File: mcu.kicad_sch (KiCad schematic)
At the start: 29 parts, among them J7 CONN_MCU_SERIAL, SW1 SW_RST, SW2 SW_BOOT0, U2 STM32F765IITx, Y2 25MHz

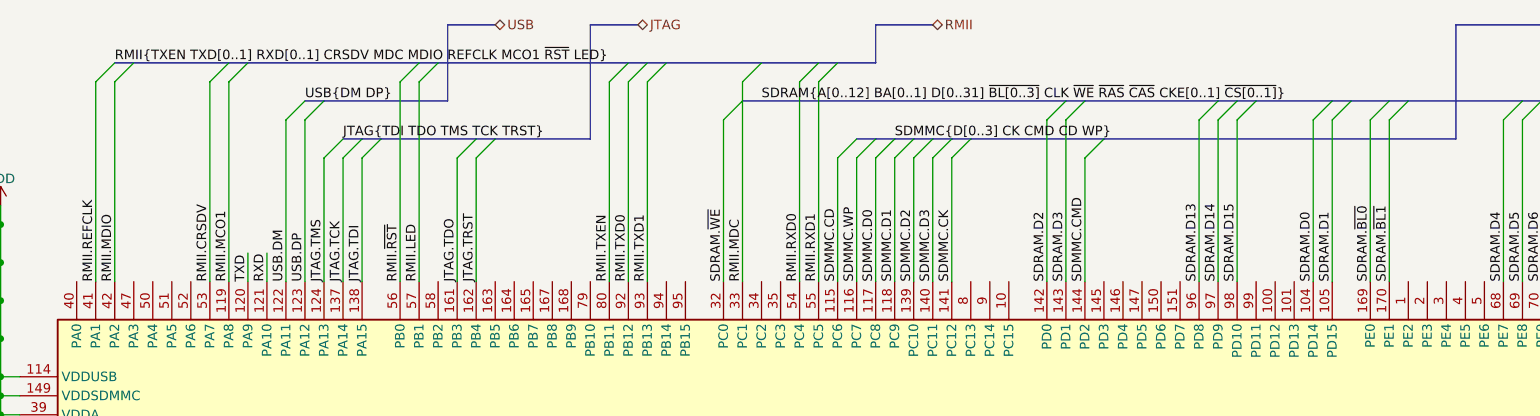
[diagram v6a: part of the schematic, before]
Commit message: Add display connector
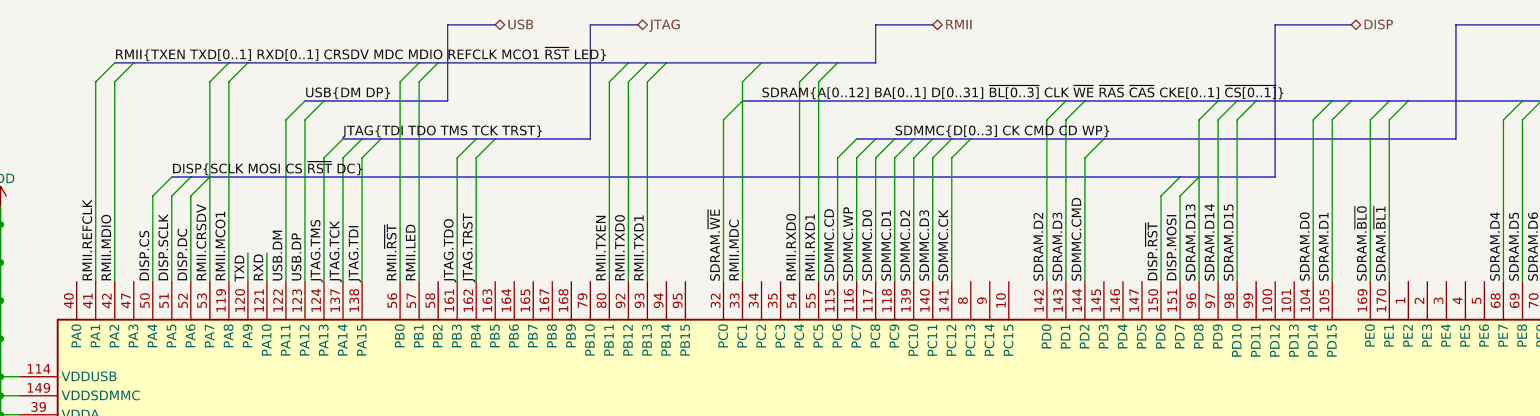
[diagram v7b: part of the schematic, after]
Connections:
- net DISP.~{RST}: now reaches U2.150 (PD6)
- net DISP.MOSI: now reaches U2.151 (PD7)
- net DISP.CS: now reaches U2.50 (PA4)
- net DISP.SCLK: now reaches U2.51 (PA5)
- net DISP.DC: now reaches U2.52 (PA6)
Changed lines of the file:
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@@
+    (stroke (width 0) (type default) (color 0 0 0 0))
+  )
+  (bus_entry (at 201.93 36.83) (size -2.54 2.54)
+    (stroke (width 0) (type default) (color 0 0 0 0))
+  )
+  (bus_entry (at 199.39 36.83) (size -2.54 2.54)
     (stroke (width 0) (type default) (color 0 0 0 0))
   )
@@
     (stroke (width 0) (type default) (color 0 0 0 0))
   )
+  (bus_entry (at 69.85 36.83) (size -2.54 2.54)
+    (stroke (width 0) (type default) (color 0 0 0 0))
+  )
   (bus_entry (at 189.23 31.75) (size -2.54 2.54)
     (stroke (width 0) (type default) (color 0 0 0 0))
@@
     (stroke (width 0) (type default) (color 0 0 0 0))
   )
+  (bus_entry (at 64.77 36.83) (size -2.54 2.54)
+    (stroke (width 0) (type default) (color 0 0 0 0))
+  )
   (bus_entry (at 153.67 144.78) (size 2.54 2.54)
     (stroke (width 0) (type default) (color 0 0 0 0))
@@
     (stroke (width 0) (type default) (color 0 0 0 0))
   )
+  (bus_entry (at 67.31 36.83) (size -2.54 2.54)
+    (stroke (width 0) (type default) (color 0 0 0 0))
+  )
   (bus_entry (at 158.75 31.75) (size -2.54 2.54)
     (stroke (width 0) (type default) (color 0 0 0 0))
@@
     (stroke (width 0) (type default) (color 0 0 0 0))
   )
-  (wire (pts (xy 69.85 24.13) (xy 69.85 50.8))
+  (wire (pts (xy 69.85 24.13) (xy 69.85 36.83))
     (stroke (width 0) (type default) (color 0 0 0 0))
   )
@@
     (stroke (width 0) (type default) (color 0 0 0 0))
   )
+  (wire (pts (xy 62.23 39.37) (xy 62.23 50.8))
+    (stroke (width 0) (type default) (color 0 0 0 0))
+  )
   (wire (pts (xy 22.86 78.74) (xy 25.4 78.74))
     (stroke (width 0) (type default) (color 0 0 0 0))
@@
     (stroke (width 0) (type default) (color 0 0 0 0))
   )
+  (bus (pts (xy 201.93 36.83) (xy 212.09 36.83))
+    (stroke (width 0) (type default) (color 0 0 0 0))
+  )
   (wire (pts (xy 191.77 124.46) (xy 191.77 144.78))
     (stroke (width 0) (type default) (color 0 0 0 0))
@@
     (stroke (width 0) (type default) (color 0 0 0 0))
   )
+  (wire (pts (xy 199.39 39.37) (xy 199.39 50.8))
+    (stroke (width 0) (type default) (color 0 0 0 0))
+  )
   (wire (pts (xy 22.86 104.14) (xy 30.48 104.14))
     (stroke (width 0) (type default) (color 0 0 0 0))
   )
+  (bus (pts (xy 67.31 36.83) (xy 69.85 36.83))
+    (stroke (width 0) (type default) (color 0 0 0 0))
+  )
   (wire (pts (xy 38.1 63.5) (xy 41.91 63.5))
     (stroke (width 0) (type default) (color 0 0 0 0))
@@
     (stroke (width 0) (type default) (color 0 0 0 0))
   )
+  (wire (pts (xy 64.77 39.37) (xy 64.77 50.8))
+    (stroke (width 0) (type default) (color 0 0 0 0))
+  )
   (wire (pts (xy 57.15 24.13) (xy 57.15 50.8))
     (stroke (width 0) (type default) (color 0 0 0 0))
@@
     (stroke (width 0) (type default) (color 0 0 0 0))
   )
-  (wire (pts (xy 201.93 29.21) (xy 201.93 50.8))
+  (wire (pts (xy 201.93 29.21) (xy 201.93 36.83))
     (stroke (width 0) (type default) (color 0 0 0 0))
   )
@@
     (stroke (width 0) (type default) (color 0 0 0 0))
   )
+  (bus (pts (xy 69.85 36.83) (xy 199.39 36.83))
+    (stroke (width 0) (type default) (color 0 0 0 0))
+  )
   (wire (pts (xy 166.37 124.46) (xy 166.37 144.78))
     (stroke (width 0) (type default) (color 0 0 0 0))
@@
     (stroke (width 0) (type default) (color 0 0 0 0))
   )
+  (bus (pts (xy 212.09 36.83) (xy 212.09 16.51))
+    (stroke (width 0) (type default) (color 0 0 0 0))
+  )
   (wire (pts (xy 252.73 124.46) (xy 252.73 144.78))
     (stroke (width 0) (type default) (color 0 0 0 0))
@@
     (stroke (width 0) (type default) (color 0 0 0 0))
   )
+  (wire (pts (xy 201.93 36.83) (xy 201.93 50.8))
+    (stroke (width 0) (type default) (color 0 0 0 0))
+  )
   (wire (pts (xy 82.55 29.21) (xy 82.55 50.8))
     (stroke (width 0) (type default) (color 0 0 0 0))
@@
     (stroke (width 0) (type default) (color 0 0 0 0))
   )
+  (bus (pts (xy 212.09 16.51) (xy 222.25 16.51))
+    (stroke (width 0) (type default) (color 0 0 0 0))
+  )
   (wire (pts (xy 234.95 124.46) (xy 234.95 144.78))
     (stroke (width 0) (type default) (color 0 0 0 0))
@@
     (stroke (width 0) (type default) (color 0 0 0 0))
   )
+  (bus (pts (xy 199.39 36.83) (xy 201.93 36.83))
+    (stroke (width 0) (type default) (color 0 0 0 0))
+  )
   (wire (pts (xy 27.94 151.13) (xy 27.94 171.45))
     (stroke (width 0) (type default) (color 0 0 0 0))
@@
     (stroke (width 0) (type default) (color 0 0 0 0))
   )
+  (wire (pts (xy 196.85 39.37) (xy 196.85 50.8))
+    (stroke (width 0) (type default) (color 0 0 0 0))
+  )
   (bus (pts (xy 229.87 26.67) (xy 245.11 26.67))
     (stroke (width 0) (type default) (color 0 0 0 0))
@@
     (stroke (width 0) (type default) (color 0 0 0 0))
   )
+  (wire (pts (xy 67.31 39.37) (xy 67.31 50.8))
+    (stroke (width 0) (type default) (color 0 0 0 0))
+  )
   (wire (pts (xy 41.91 66.04) (xy 41.91 68.58))
     (stroke (width 0) (type default) (color 0 0 0 0))
@@
     (stroke (width 0) (type default) (color 0 0 0 0))
   )
+  (bus (pts (xy 64.77 36.83) (xy 67.31 36.83))
+    (stroke (width 0) (type default) (color 0 0 0 0))
+  )
   (bus (pts (xy 158.75 147.32) (xy 161.29 147.32))
     (stroke (width 0) (type default) (color 0 0 0 0))
@@
     (stroke (width 0) (type default) (color 0 0 0 0))
   )
+  (wire (pts (xy 69.85 36.83) (xy 69.85 50.8))
+    (stroke (width 0) (type default) (color 0 0 0 0))
+  )
   (wire (pts (xy 270.51 78.74) (xy 274.32 78.74))
     (stroke (width 0) (type default) (color 0 0 0 0))
@@
     (effects (font (size 1.27 1.27)) (justify left bottom))
   )
+  (label "DISP{SCLK MOSI CS ~{RST} DC}" (at 64.77 36.83 0)
+    (effects (font (size 1.27 1.27)) (justify left bottom))
+  )
   (label "RMII.RXD0" (at 148.59 50.8 90)
     (effects (font (size 1.27 1.27)) (justify left bottom))
@@
   )
   (label "SDRAM.D7" (at 250.19 50.8 90)
+    (effects (font (size 1.27 1.27)) (justify left bottom))
+  )
+  (label "DISP.~{RST}" (at 196.85 50.8 90)
+    (effects (font (size 1.27 1.27)) (justify left bottom))
+  )
+  (label "DISP.MOSI" (at 199.39 50.8 90)
     (effects (font (size 1.27 1.27)) (justify left bottom))
   )
@@
     (effects (font (size 1.27 1.27)) (justify right bottom))
   )
+  (label "DISP.SCLK" (at 64.77 50.8 90)
+    (effects (font (size 1.27 1.27)) (justify left bottom))
+  )
   (label "SDRAM.D5" (at 245.11 50.8 90)
     (effects (font (size 1.27 1.27)) (justify left bottom))
@@
     (effects (font (size 1.27 1.27)) (justify right bottom))
   )
+  (label "DISP.DC" (at 67.31 50.8 90)
+    (effects (font (size 1.27 1.27)) (justify left bottom))
+  )
   (label "SDRAM.D22" (at 173.99 124.46 270)
     (effects (font (size 1.27 1.27)) (justify right bottom))
@@
   )
   (label "SDRAM.D10" (at 257.81 50.8 90)
+    (effects (font (size 1.27 1.27)) (justify left bottom))
+  )
+  (label "DISP.CS" (at 62.23 50.8 90)
     (effects (font (size 1.27 1.27)) (justify left bottom))
   )
@@
     (effects (font (size 1.27 1.27)) (justify left))
   )
+  (hierarchical_label "DISP" (shape bidirectional) (at 222.25 16.51 0)
+    (effects (font (size 1.27 1.27)) (justify left))
+  )

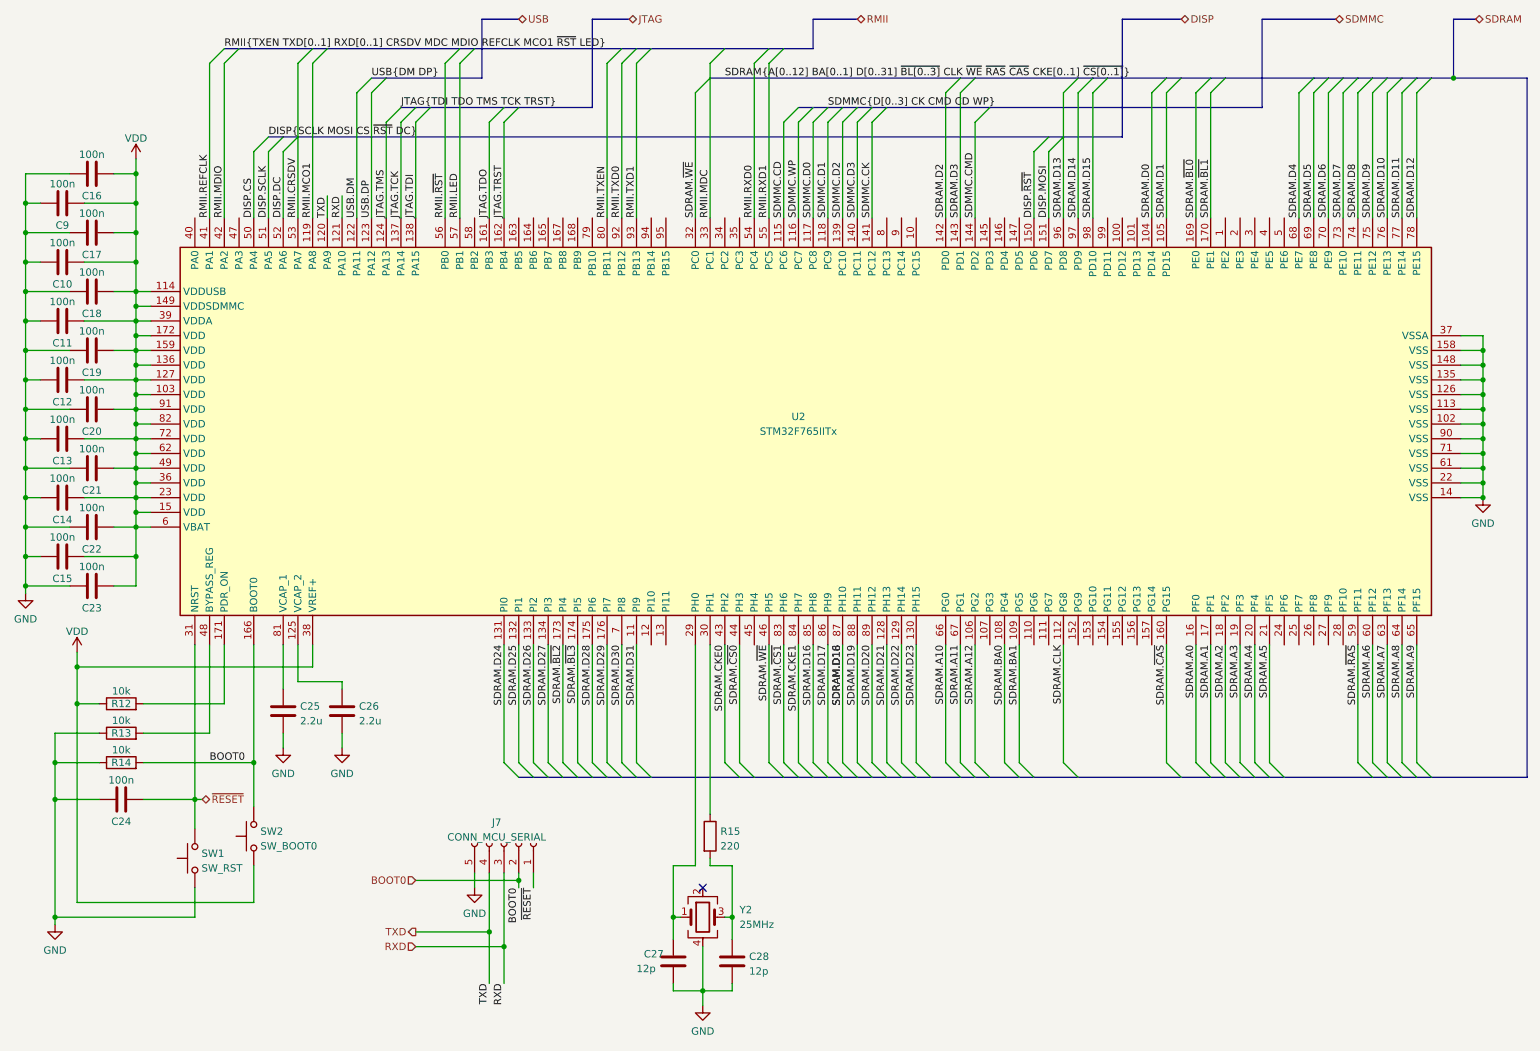
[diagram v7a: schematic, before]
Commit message: Add extension connector, LEDs, buttons
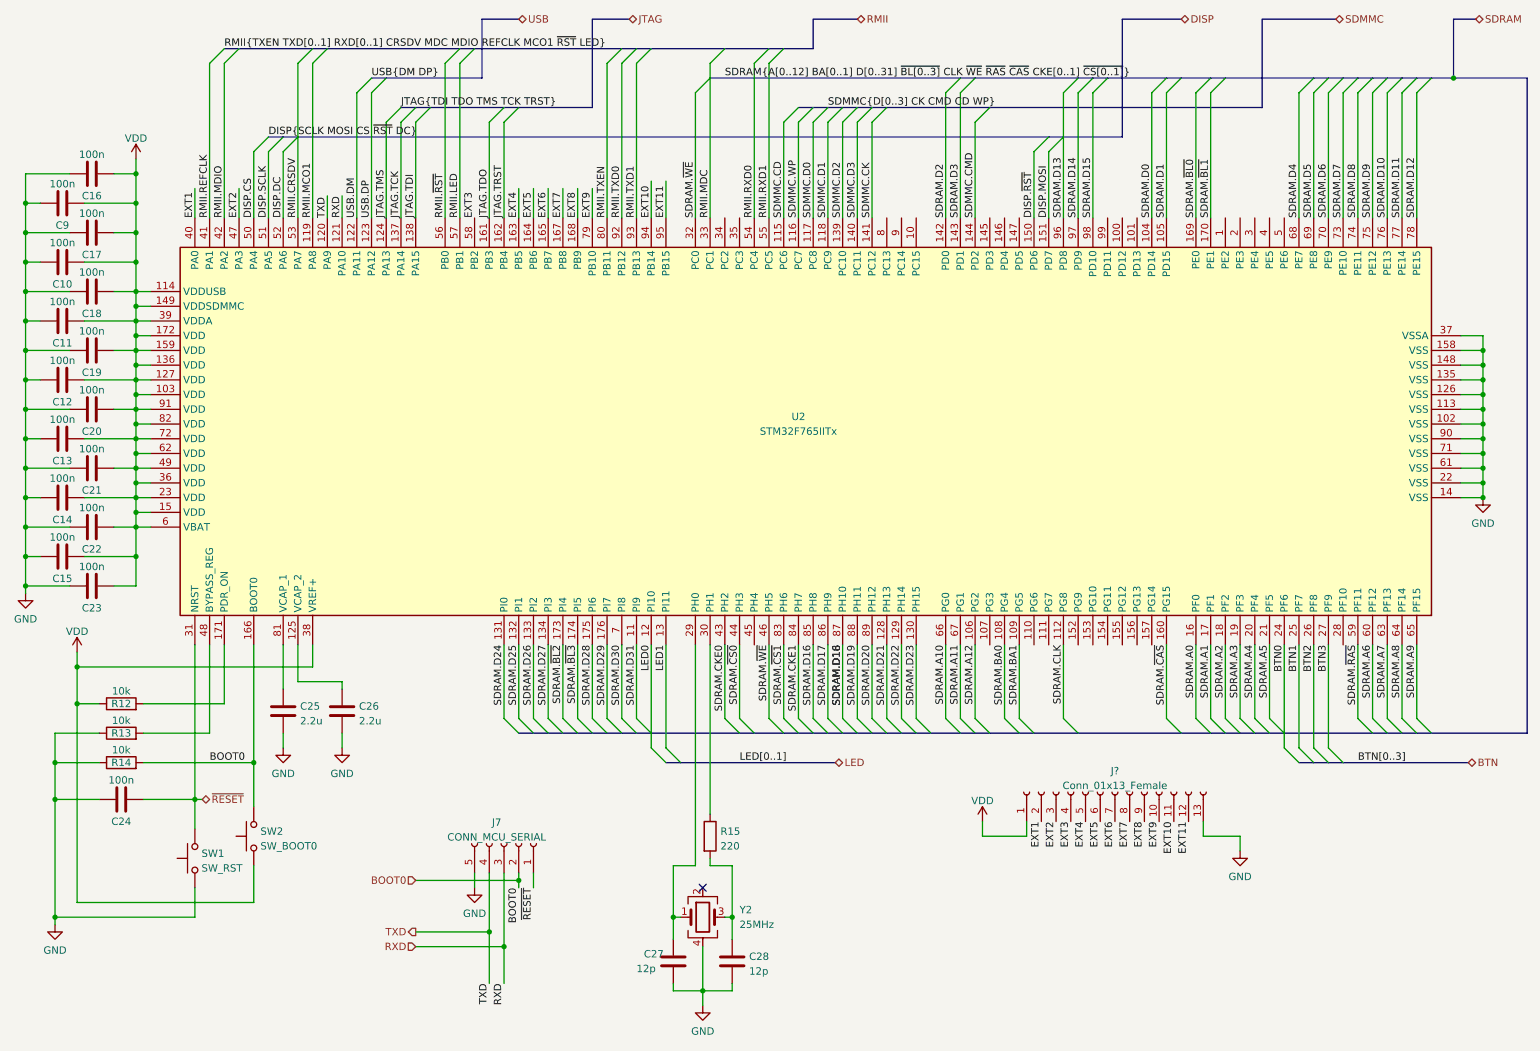
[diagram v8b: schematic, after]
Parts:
- added J?: Conn_01x13_Female, symbol Connector:Conn_01x13_Female
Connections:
- net GND: now also J?.13 (Pin_13)
- net VDD: now also J?.1 (Pin_1)
- net LED0: now reaches U2.12 (PI10)
- net LED1: now reaches U2.13 (PI11)
- net EXT4: now reaches U2.163 (PB5)
- net EXT4: now also J?.5 (Pin_5)
- net EXT5: now reaches U2.164 (PB6)
- net EXT5: now also J?.6 (Pin_6)
- net EXT6: now reaches U2.165 (PB7)
- net EXT6: now also J?.7 (Pin_7)
- net EXT7: now reaches U2.167 (PB8)
- net EXT7: now also J?.8 (Pin_8)
- net EXT8: now reaches U2.168 (PB9)
- net EXT8: now also J?.9 (Pin_9)
- net BTN0: now reaches U2.24 (PF6)
- net BTN1: now reaches U2.25 (PF7)
- net BTN2: now reaches U2.26 (PF8)
- net BTN3: now reaches U2.27 (PF9)
- net EXT1: now reaches U2.40 (PA0)
- net EXT1: now also J?.2 (Pin_2)
- net EXT2: now reaches U2.47 (PA3)
- net EXT2: now also J?.3 (Pin_3)
- net EXT3: now reaches U2.58 (PB2)
- net EXT3: now also J?.4 (Pin_4)
- net EXT9: now reaches U2.79 (PB10)
- net EXT9: now also J?.10 (Pin_10)
- net EXT10: now reaches U2.94 (PB14)
- net EXT10: now also J?.11 (Pin_11)
- net EXT11: now reaches U2.95 (PB15)
- net EXT11: now also J?.12 (Pin_12)
